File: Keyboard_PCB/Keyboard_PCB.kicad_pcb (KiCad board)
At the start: 6 copper layers, 51 parts, among them J1 Conn_ARM_SWD_TagConnect_TC2030, J2 CH_USB_C, SW1 BOOT, SW10 7, SW11 8, SW12 9, SW13 10, SW14 11, SW2 NRST, SW3 0, SW4 1, SW5 2, SW6 3, SW7 4, SW8 5, SW9 6, U1 EMMC32G-TS0A-01002, U2 STM32U385VGI6, U3 CC2500, U4 USBLC6-2SC6, U5 ISL91127IRAZ, Y1 25MHz, Y2 32.786KHz

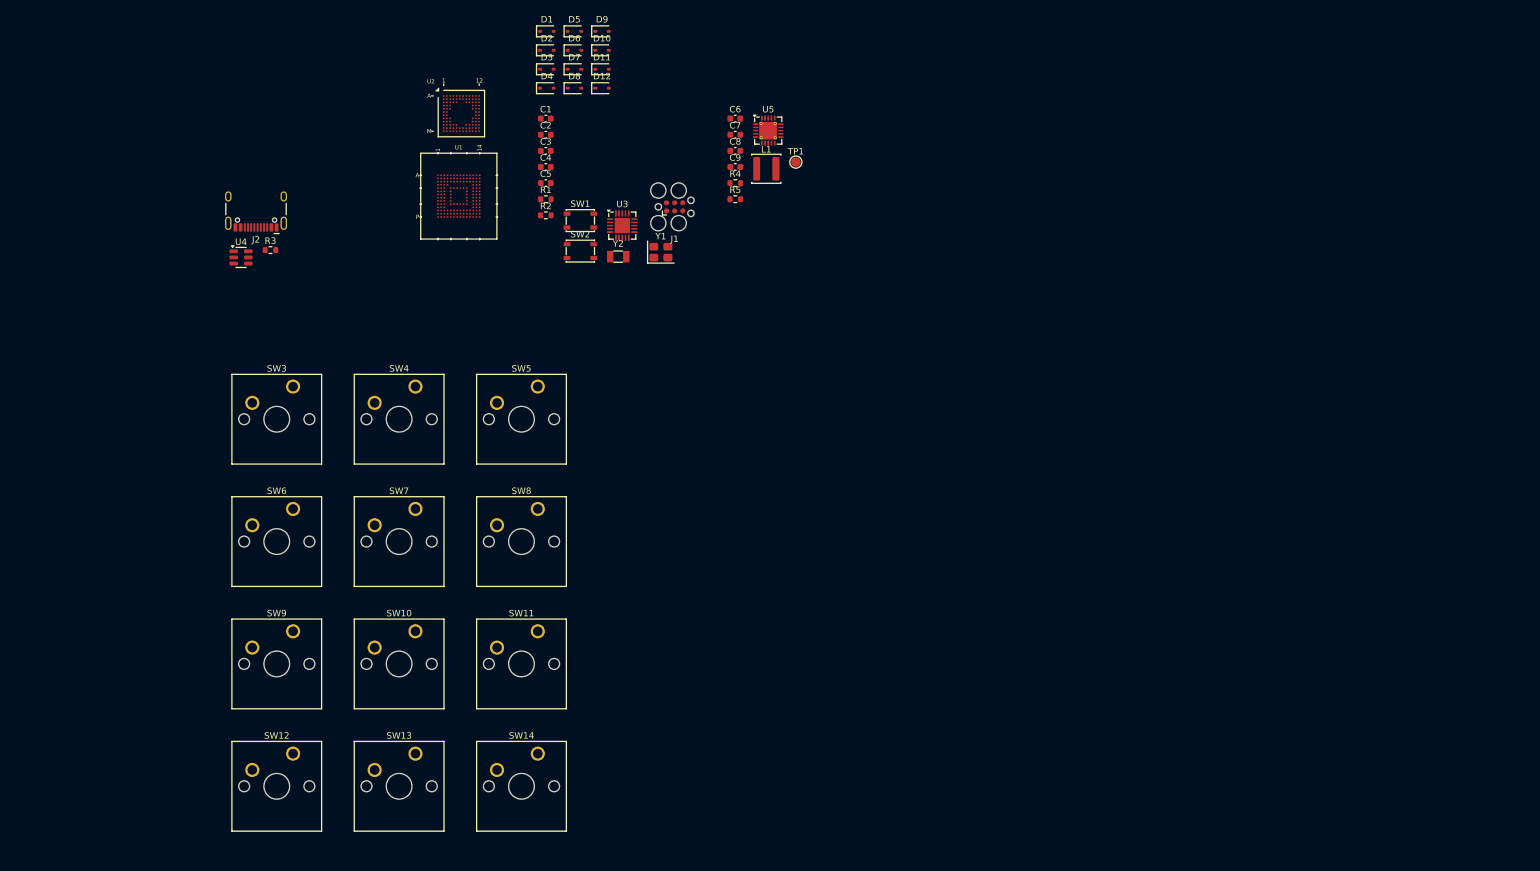
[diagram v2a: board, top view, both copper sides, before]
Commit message: Schematic done
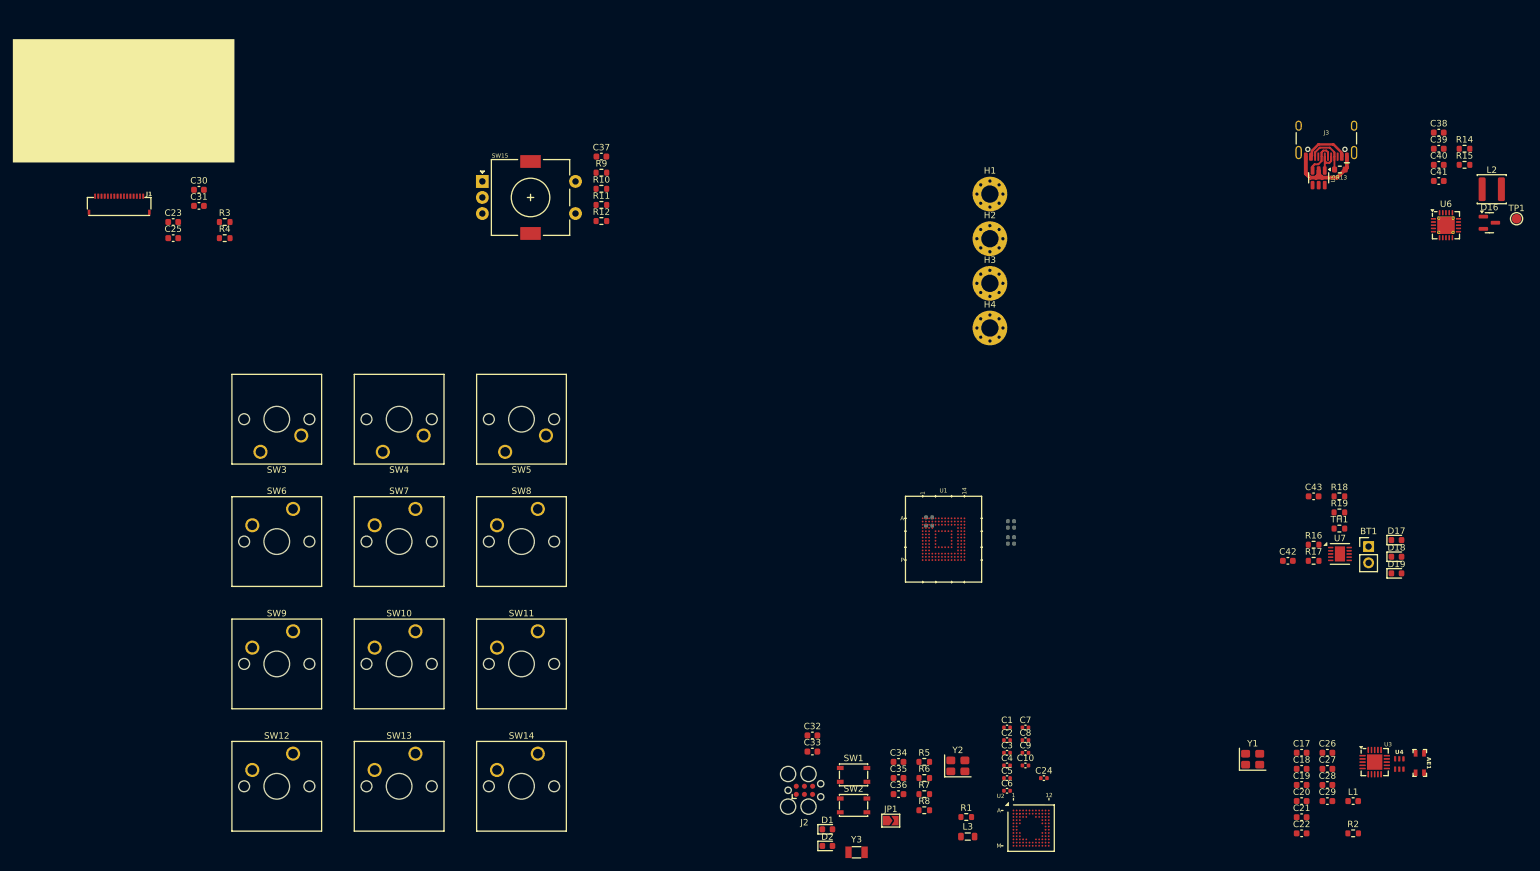
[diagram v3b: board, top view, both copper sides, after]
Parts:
- removed D10, D11, D12, D3, D4, D5, D6, D7, D8, D9: D_Small, Diode_SMD:D_SOD-323
- added AE1: 2450AT18D0100, Marijn:2450AT18D0100, F.Cu at (281.3, 149.2)
- added BT1: APP, Connector_PinHeader_2.54mm:PinHeader_1x02_P2.54mm_Vertical, F.Cu at (273.3, 115.4)
- added C10: 10u, Capacitor_SMD:C_0402_1005Metric, F.Cu at (219.9, 149.5)
- added C11: 4u7, Capacitor_SMD:C_0402_1005Metric, B.Cu at (217.6, 114.0)
- added C12: 4u7, Capacitor_SMD:C_0402_1005Metric, B.Cu at (217.6, 111.5)
- added C13: 4u7, Capacitor_SMD:C_0402_1005Metric, B.Cu at (204.9, 110.9)
- added C14: 100n, Capacitor_SMD:C_0402_1005Metric, B.Cu at (217.6, 115.0)
- added C15: 100n, Capacitor_SMD:C_0402_1005Metric, B.Cu at (217.6, 112.5)
- added C16: 100n, Capacitor_SMD:C_0402_1005Metric, B.Cu at (204.9, 112.2)
- added C17: 220p, Capacitor_SMD:C_0603_1608Metric, F.Cu at (262.9, 147.6)
- added C18: 100n, Capacitor_SMD:C_0603_1608Metric, F.Cu at (262.9, 150.1)
- added C19: 100n, Capacitor_SMD:C_0603_1608Metric, F.Cu at (262.9, 152.6)
- added C20: 220p, Capacitor_SMD:C_0603_1608Metric, F.Cu at (262.9, 155.1)
- added C21: 220p, Capacitor_SMD:C_0603_1608Metric, F.Cu at (262.9, 157.6)
- added C22: 100n, Capacitor_SMD:C_0603_1608Metric, F.Cu at (262.9, 160.1)
- added C23: 1u, Capacitor_SMD:C_0603_1608Metric, F.Cu at (87.2, 64.9)
- added C24: 4u7, Capacitor_SMD:C_0402_1005Metric, F.Cu at (222.7, 151.5)
- added C25: 1u, Capacitor_SMD:C_0603_1608Metric, F.Cu at (87.2, 67.4)
- added C26: 22p, Capacitor_SMD:C_0603_1608Metric, F.Cu at (266.9, 147.6)
- added C27: 100n, Capacitor_SMD:C_0603_1608Metric, F.Cu at (266.9, 150.1)
- added C28: 15p, Capacitor_SMD:C_0603_1608Metric, F.Cu at (266.9, 152.6)
- added C29: 15p, Capacitor_SMD:C_0603_1608Metric, F.Cu at (266.9, 155.1)
- added C30: 10u, Capacitor_SMD:C_0603_1608Metric, F.Cu at (91.2, 59.9)
- added C31: 10u, Capacitor_SMD:C_0603_1608Metric, F.Cu at (91.2, 62.4)
- added C32: 100n, Capacitor_SMD:C_0603_1608Metric, F.Cu at (186.7, 144.9)
- added C33: 12p, Capacitor_SMD:C_0603_1608Metric, F.Cu at (186.7, 147.4)
- added C34: 12p, Capacitor_SMD:C_0603_1608Metric, F.Cu at (200.1, 149.0)
- added C35: 12p, Capacitor_SMD:C_0603_1608Metric, F.Cu at (200.1, 151.5)
- added C36: 12p, Capacitor_SMD:C_0603_1608Metric, F.Cu at (200.1, 154.0)
- added C37: 100n, Capacitor_SMD:C_0603_1608Metric, F.Cu at (153.8, 54.7)
- added C38: 10u, Capacitor_SMD:C_0603_1608Metric, F.Cu at (284.2, 51.0)
- added C39: 56p, Capacitor_SMD:C_0603_1608Metric, F.Cu at (284.2, 53.5)
- added C40: 22u, Capacitor_SMD:C_0603_1608Metric, F.Cu at (284.2, 56.0)
- added C41: 22u, Capacitor_SMD:C_0603_1608Metric, F.Cu at (284.2, 58.5)
- added C42: 1u, Capacitor_SMD:C_0603_1608Metric, F.Cu at (260.7, 117.7)
- added C43: 1u, Capacitor_SMD:C_0603_1608Metric, F.Cu at (264.7, 107.6)
- added D16: BAT54C, Package_TO_SOT_SMD:SOT-23, F.Cu at (292.1, 65.0)
- added D17: STAT1, LED_SMD:LED_0603_1608Metric, F.Cu at (277.6, 114.4)
- added D18: STAT2, LED_SMD:LED_0603_1608Metric, F.Cu at (277.6, 117.0)
- added D19: PG, LED_SMD:LED_0603_1608Metric, F.Cu at (277.6, 119.6)
- added H1: MountingHole_Pad, MountingHole:MountingHole_2.7mm_M2.5_Pad_Via, F.Cu at (214.3, 60.6)
- added H2: MountingHole_Pad, MountingHole:MountingHole_2.7mm_M2.5_Pad_Via, F.Cu at (214.3, 67.5)
- added H3: MountingHole_Pad, MountingHole:MountingHole_2.7mm_M2.5_Pad_Via, F.Cu at (214.3, 74.5)
- added H4: MountingHole_Pad, MountingHole:MountingHole_2.7mm_M2.5_Pad_Via, F.Cu at (214.3, 81.4)
- added J3: CH_USB_C, Connector_USB:USB_C_Receptacle_HCTL_HC-TYPE-C-16P-01A, F.Cu at (266.7, 51.0)
- added JP1: PWR_LED_EN, Jumper:SolderJumper-2_P1.3mm_Open_TrianglePad1.0x1.5mm, F.Cu at (198.9, 158.1)
- added L2: 1u, Inductor_SMD:L_APV_ANR4018, F.Cu at (292.5, 59.8)
- added L3: 10u, Inductor_SMD:L_0805_2012Metric, F.Cu at (210.9, 160.6)
- added R10: 10k, Resistor_SMD:R_0603_1608Metric, F.Cu at (153.8, 59.8)
- added R11: 10k, Resistor_SMD:R_0603_1608Metric, F.Cu at (153.8, 62.3)
- added R12: 10k, Resistor_SMD:R_0603_1608Metric, F.Cu at (153.8, 64.8)
- added R13: 5k1, Resistor_SMD:R_0603_1608Metric, F.Cu at (268.8, 56.8)
- added R14: 1M, Resistor_SMD:R_0603_1608Metric, F.Cu at (288.2, 53.5)
- added R15: 320k, Resistor_SMD:R_0603_1608Metric, F.Cu at (288.2, 56.0)
- added R16: 470, Resistor_SMD:R_0603_1608Metric, F.Cu at (264.7, 115.2)
- added R17: 470, Resistor_SMD:R_0603_1608Metric, F.Cu at (264.7, 117.7)
- added R18: 470, Resistor_SMD:R_0603_1608Metric, F.Cu at (268.7, 107.6)
- added R19: 10k, Resistor_SMD:R_0603_1608Metric, F.Cu at (268.7, 110.1)
- added R6: 5k1, Resistor_SMD:R_0603_1608Metric, F.Cu at (204.1, 151.5)
- added R7: 10k, Resistor_SMD:R_0603_1608Metric, F.Cu at (204.1, 154.0)
- added R8: 1k, Resistor_SMD:R_0603_1608Metric, F.Cu at (204.1, 156.5)
- added R9: 10k, Resistor_SMD:R_0603_1608Metric, F.Cu at (153.8, 57.2)
- added SW15: EC11E15244G1, Marijn:EC11E_rotary_MP_pads, F.Cu at (135.3, 58.6)
- added TH1: 10k, Resistor_SMD:R_0603_1608Metric, F.Cu at (268.7, 112.7)
- added U6: ISL91127IRAZ, Package_DFN_QFN:QFN-20-1EP_4x4mm_P0.5mm_EP2.7x2.7mm_ThermalVias, F.Cu at (285.3, 65.4)
- added U7: MCP73833, Package_DFN_QFN:DFN-10-1EP_3x3mm_P0.5mm_EP1.58x2.35mm, F.Cu at (268.8, 116.6)
- added Y3: 32.786KHz, Crystal:Crystal_SMD_3215-2Pin_3.2x1.5mm, F.Cu at (193.6, 163.1)
- C1: footprint Capacitor_SMD:C_0603_1608Metric -> Capacitor_SMD:C_0402_1005Metric
- C2, C3, C5: value 12p -> 100n; footprint Capacitor_SMD:C_0603_1608Metric -> Capacitor_SMD:C_0402_1005Metric
- C4: value 12p -> 1u; footprint Capacitor_SMD:C_0603_1608Metric -> Capacitor_SMD:C_0402_1005Metric
- C6: value 10u -> 100n; footprint Capacitor_SMD:C_0603_1608Metric -> Capacitor_SMD:C_0402_1005Metric
- C7: value 56p -> 100n; footprint Capacitor_SMD:C_0603_1608Metric -> Capacitor_SMD:C_0402_1005Metric
- C8, C9: value 22u -> 100n; footprint Capacitor_SMD:C_0603_1608Metric -> Capacitor_SMD:C_0402_1005Metric
- D1: value D_Small -> PWR; footprint Diode_SMD:D_SOD-323 -> LED_SMD:LED_0603_1608Metric
- D2: value D_Small -> CH_STATUS; footprint Diode_SMD:D_SOD-323 -> LED_SMD:LED_0603_1608Metric
- J1: value Conn_ARM_SWD_TagConnect_TC2030 -> ~; footprint Connector:Tag-Connect_TC2030-IDC-FP_2x03_P1.27mm_Vertical -> Marijn:FFC2B28-16-G
- J2: value CH_USB_C -> Conn_ARM_SWD_TagConnect_TC2030; footprint Connector_USB:USB_C_Receptacle_HCTL_HC-TYPE-C-16P-01A -> Connector:Tag-Connect_TC2030-IDC-FP_2x03_P1.27mm_Vertical
- L1: value 1u -> 10n; footprint Inductor_SMD:L_APV_ANR4018 -> Inductor_SMD:L_0603_1608Metric
- R2: value 10k -> 56k
- R4: value 1M -> 680K
- R5: value 320k -> 10k
- U4: value USBLC6-2SC6 -> 2450BM15B0003001E; footprint Package_TO_SOT_SMD:SOT-23-6 -> Marijn:2450BM15B0003001E
- U5: value ISL91127IRAZ -> USBLC6-2SC6; footprint Package_DFN_QFN:QFN-20-1EP_4x4mm_P0.5mm_EP2.7x2.7mm_ThermalVias -> Package_TO_SOT_SMD:SOT-23-6
- Y1: value 25MHz -> 26MHz
- Y2: value 32.786KHz -> 25MHz; footprint Crystal:Crystal_SMD_3215-2Pin_3.2x1.5mm -> Crystal:Crystal_SMD_3225-4Pin_3.2x2.5mm
- moved U4 196.8 mm to (278.1, 149.3)
- moved R2 158.3 mm to (270.9, 160.1)
- moved U3 143.9 mm to (274.2, 149.0)
- moved U2 142.3 mm to (220.7, 159.3)
- moved L1 134.3 mm to (270.9, 155.1)
- moved D1 131.7 mm to (189.0, 159.5)
- moved D2 131.3 mm to (189.0, 162.1)
- moved J2 125.1 mm to (185.5, 153.4), turned to 0 degrees
- moved Y1 121.3 mm to (255.2, 148.6)
- moved C1 118.9 mm to (217.0, 143.6)
- moved C2 118.5 mm to (217.0, 145.6)
- moved C3 118.1 mm to (217.0, 147.6)
- moved C4 117.6 mm to (217.0, 149.5)
- moved C5 117.2 mm to (217.0, 151.5)
- moved R1 116.3 mm to (210.6, 157.6)
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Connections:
- C1 pad 2: /NRST -> +3V3
- C2 pad 2: /HSE_I -> +3V3
- C3 pad 2: /HSE_O -> +3.3VA
- C4 pad 2: /LSE_I -> +3.3VA
- C5 pad 2: /LSE_O -> +3V3
- C6 pad 1: /PWR/VBUS -> GND
- C6 pad 2: GND -> +3V3
- C7 pad 1: +3V3 -> GND
- C7 pad 2: Net-(U5-FB) -> +3V3
- C8 pad 1: +3V3 -> GND
- C8 pad 2: GND -> +3V3
- C9 pad 1: +3V3 -> GND
- C9 pad 2: GND -> +3V3
- D1 pad 1: /ROW_0 -> GND
- D2 pad 1: /ROW_0 -> /STATUS
- J1 pad 1: +3V3 -> Net-(C23-Pad1)
- J1 pad 2: /SWDIO -> Net-(C23-Pad2)
- J1 pad 3: /NRST -> Net-(C25-Pad1)
- J1 pad 4: /SWCLK -> Net-(C25-Pad2)
- J1 pad 5: GND -> +3V3
- J1 pad 6: /SWO -> GND
- L1 pad 1: Net-(L1-Pad1) -> Net-(U3-RF_P)
- L1 pad 2: Net-(L1-Pad2) -> Net-(U3-RF_N)
- R1 pad 1: /NRST -> /BAT
- R1 pad 2: +3V3 -> Net-(U2-PC0)
- R2 pad 2: /BOOT -> Net-(U3-RBIAS)
- R3 pad 1: Net-(J2-CC1) -> GND
- R3 pad 2: GND -> /OLED_RST
- R4 pad 1: +3V3 -> Net-(J1-Pad13)
- R4 pad 2: Net-(U5-FB) -> GND
- R5 pad 1: GND -> /NRST
- R5 pad 2: Net-(U5-FB) -> +3V3
- SW3 pad 2: Net-(D1-A) -> Net-(D3-A)
- SW4 pad 2: Net-(D2-A) -> Net-(D4-A)
- U1 pad C2: unconnected-(U1-VDD_i-PadC2) -> Net-(U1-VDD_i)
- U2 pad A9: unconnected-(U2-PA15-PadA9) -> /STATUS
- U2 pad C11: unconnected-(U2-VDDUSB-PadC11) -> +3V3
- U2 pad C4: unconnected-(U2-VDD-PadC4) -> +3V3
- U2 pad D3: unconnected-(U2-VSS-PadD3) -> GND
- U2 pad E2: unconnected-(U2-VBAT-PadE2) -> +3V3
- U2 pad E3: unconnected-(U2-VSS-PadE3) -> GND
- U2 pad F11: unconnected-(U2-VSS-PadF11) -> GND
- U2 pad F12: unconnected-(U2-VSS-PadF12) -> GND
- U2 pad F2: unconnected-(U2-VSS-PadF2) -> GND
- U2 pad G11: unconnected-(U2-VDD-PadG11) -> +3V3
- U2 pad G12: unconnected-(U2-VDD-PadG12) -> +3V3
- U2 pad G2: unconnected-(U2-VDD-PadG2) -> +3V3
- U2 pad H1: unconnected-(U2-PC0-PadH1) -> Net-(U2-PC0)
- U2 pad H12: unconnected-(U2-PD13-PadH12) -> /ROT_A
- U2 pad H3: unconnected-(U2-VDD-PadH3) -> +3V3
- U2 pad J1: unconnected-(U2-VSSA-PadJ1) -> GND
- U2 pad J12: unconnected-(U2-PD10-PadJ12) -> /ROT_B
- U2 pad K1: unconnected-(U2-VREF--PadK1) -> GND
- U2 pad K11: /OLED_SPI_NSS -> unconnected-(U2-PB14-PadK11)
- U2 pad L1: unconnected-(U2-VREF+-PadL1) -> +3.3VA
- U2 pad L11: unconnected-(U2-VCAP-PadL11) -> Net-(U2-VCAP)
- U2 pad L12: unconnected-(U2-PB12-PadL12) -> /OLED_SPI_NSS
- U2 pad L2: unconnected-(U2-PA0-PadL2) -> /ROT_SW
- U2 pad M1: unconnected-(U2-VDDA-PadM1) -> +3.3VA
- U3 pad 1: /SPI_SCK -> /RF_SPI_SCK
- U3 pad 10: unconnected-(U3-XOSC_Q2-Pad10) -> Net-(U3-XOSC_Q2)
- U3 pad 11: Net-(U3-AVDD-Pad11) -> +3V3
- U3 pad 12: unconnected-(U3-RF_P-Pad12) -> Net-(U3-RF_P)
- U3 pad 13: unconnected-(U3-RF_N-Pad13) -> Net-(U3-RF_N)
- U3 pad 14: Net-(U3-AVDD-Pad11) -> +3V3
- U3 pad 15: Net-(U3-AVDD-Pad11) -> +3V3
- U3 pad 17: unconnected-(U3-RBIAS-Pad17) -> Net-(U3-RBIAS)
- U3 pad 18: unconnected-(U3-VDD_GUARD-Pad18) -> +3V3
- U3 pad 2: /SPI_MISO -> /RF_SPI_MISO
- U3 pad 20: /SPI_MOSI -> /RF_SPI_MOSI
- U3 pad 4: unconnected-(U3-DVDD-Pad4) -> +3V3
- U3 pad 5: unconnected-(U3-DCOUPL-Pad5) -> Net-(U3-DCOUPL)
- U3 pad 7: /SPI_NSS -> /RF_SPI_NSS
- U3 pad 8: unconnected-(U3-XOSC_Q1-Pad8) -> Net-(U3-XOSC_Q1)
- U3 pad 9: Net-(U3-AVDD-Pad11) -> +3V3
- U4 pad 1: Net-(J2-D--PadA7) -> Net-(AE1-FEED)
- U4 pad 2: GND -> Net-(U4-CAP)
- U4 pad 3: Net-(J2-D+-PadA6) -> Net-(U3-RF_N)
- U4 pad 4: /USB_DP -> Net-(U3-RF_P)
- U4 pad 5: /PWR/VBUS -> GND
- U4 pad 6: /USB_DN -> GND
- U5 pad 1: Net-(L1-Pad2) -> Net-(J3-D--PadA7)
- U5 pad 2: Net-(L1-Pad2) -> GND
- U5 pad 3: GND -> Net-(J3-D+-PadA6)
- U5 pad 4: Net-(L1-Pad1) -> /USB_DP
- U5 pad 5: Net-(L1-Pad1) -> /PWR/VBUS
- U5 pad 6: /PWR/VBUS -> /USB_DN
- Y1 pad 1: /HSE_I -> Net-(U3-XOSC_Q1)
- Y1 pad 3: /HSE_O -> Net-(U3-XOSC_Q2)
- Y2 pad 1: /LSE_I -> /HSE_I
- Y2 pad 2: /LSE_O -> GND
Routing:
- net GND: track 0.00 -> 14.3 mm
- net /PWR/VBUS: track 0.00 -> 7.17 mm
- net Net-(J3-CC1): track 0.00 -> 6.98 mm
- net Net-(J3-D+-PadA6): track 0.00 -> 5.67 mm
- net Net-(J3-D--PadA7): track 0.00 -> 4.74 mm

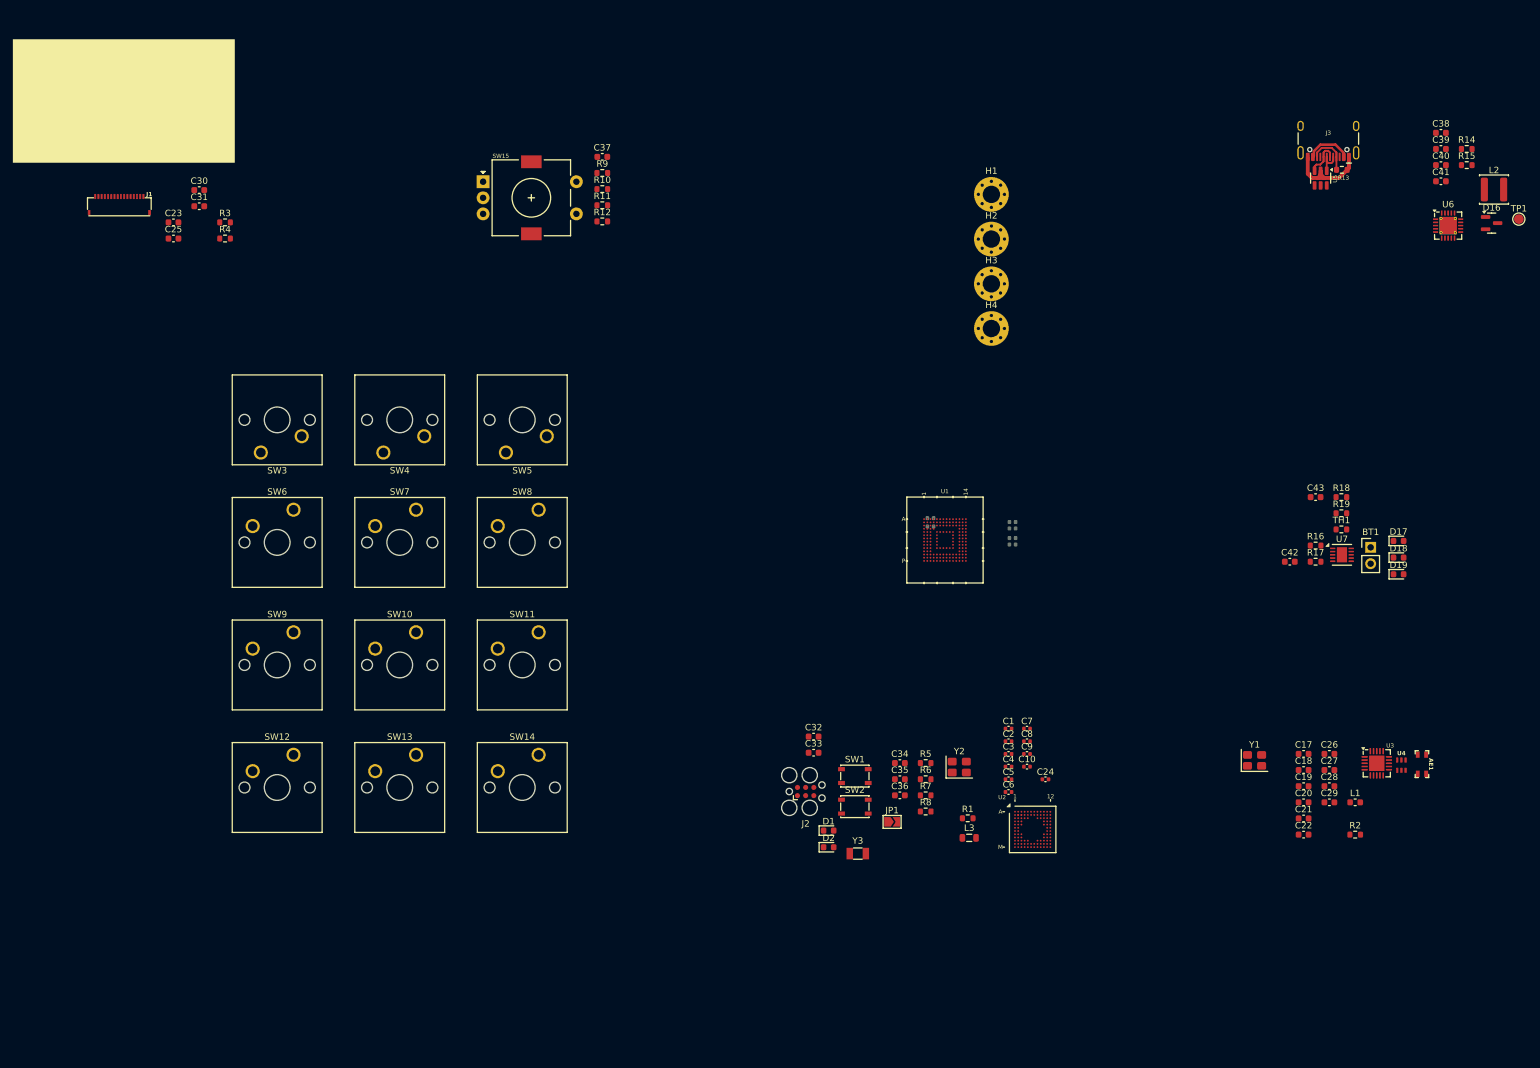
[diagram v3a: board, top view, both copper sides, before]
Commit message: eMMC routing and STM passives
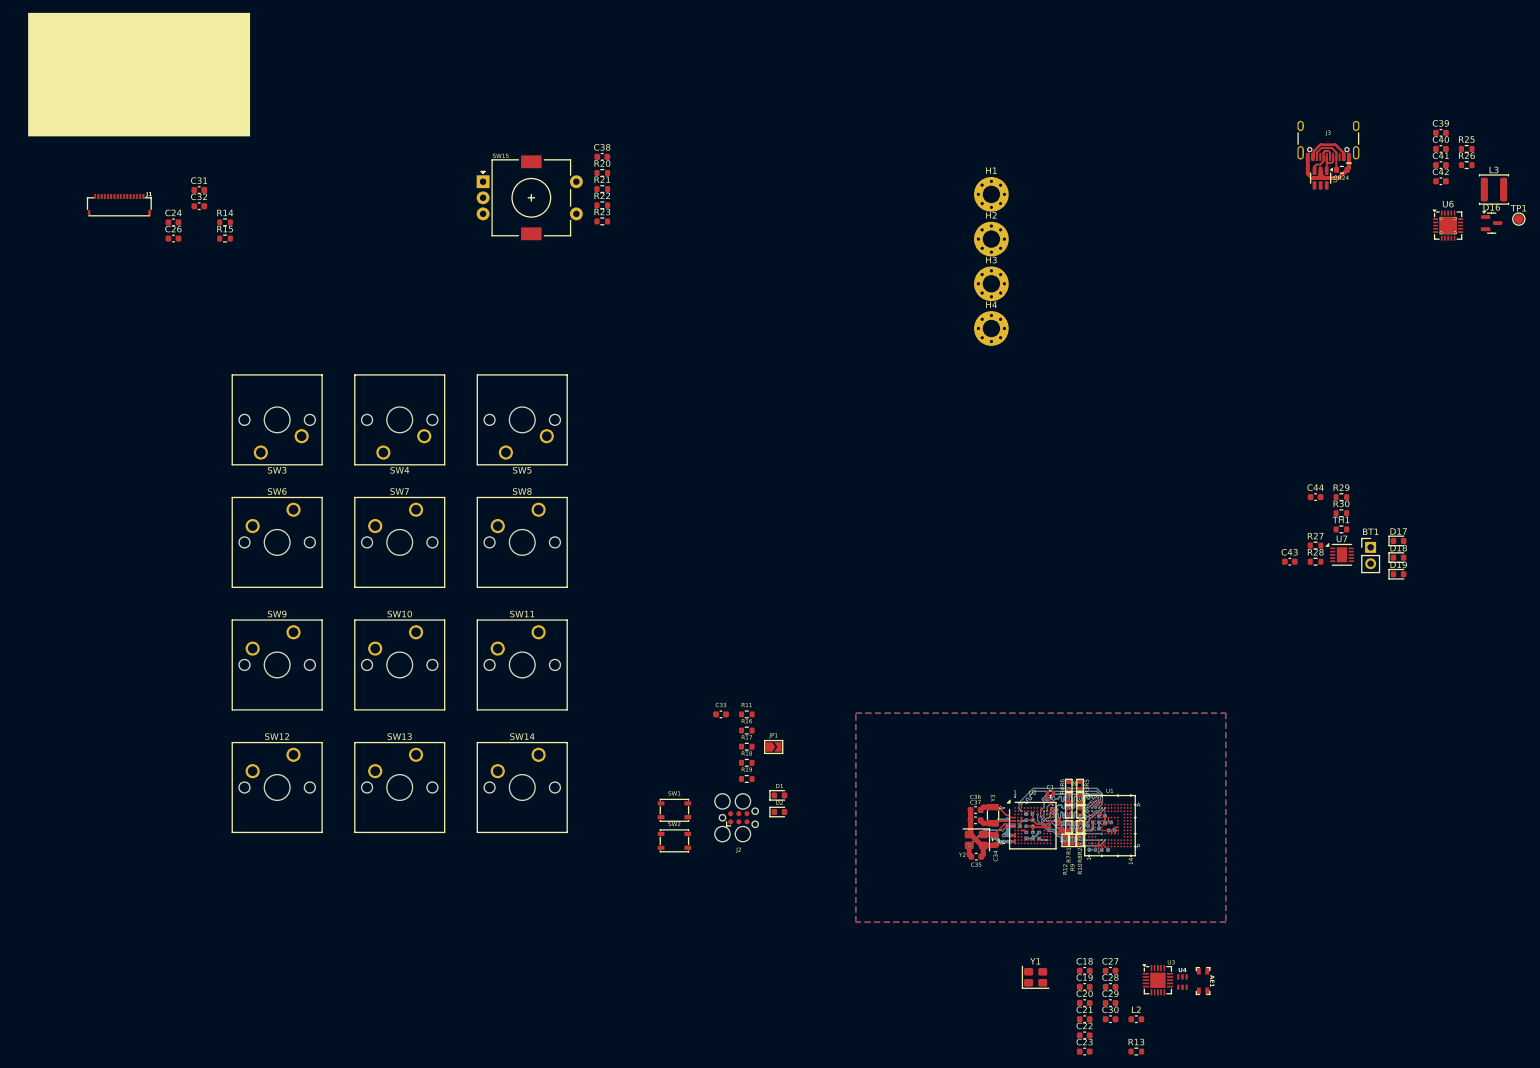
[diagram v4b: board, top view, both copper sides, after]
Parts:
- removed the C24 at (222.7, 151.5)
- removed the C32 at (186.7, 144.9)
- removed the L3 at (210.9, 160.6)
- added C17: 100n, Capacitor_SMD:C_0402_1005Metric, B.Cu at (230.6, 158.2)
- added C25: 4u7, Capacitor_SMD:C_0402_1005Metric, B.Cu at (221.8, 160.2)
- added C37: 12p, Capacitor_SMD:C_0603_1608Metric, F.Cu at (211.9, 157.9)
- added L1: 10u, Inductor_SMD:L_0805_2012Metric, B.Cu at (214.9, 159.5)
- added R10: 22, PCM_Resistor_SMD_AKL:R_0402_1005Metric, F.Cu at (228.1, 161.0)
- added R11: 10k, Resistor_SMD:R_0603_1608Metric, F.Cu at (176.3, 141.4)
- added R12: 50k, PCM_Resistor_SMD_AKL:R_0402_1005Metric, F.Cu at (225.8, 161.0)
- added R16: 10k, Resistor_SMD:R_0603_1608Metric, F.Cu at (176.3, 143.9)
- added R17: 5k1, Resistor_SMD:R_0603_1608Metric, F.Cu at (176.3, 146.4)
- added R18: 10k, Resistor_SMD:R_0603_1608Metric, F.Cu at (176.3, 148.9)
- added R19: 1k, Resistor_SMD:R_0603_1608Metric, F.Cu at (176.3, 151.5)
- added R2: 50k, PCM_Resistor_SMD_AKL:R_0402_1005Metric, F.Cu at (228.1, 156.6)
- added R3: 50k, PCM_Resistor_SMD_AKL:R_0402_1005Metric, F.Cu at (228.1, 154.5)
- added R4: 50k, PCM_Resistor_SMD_AKL:R_0402_1005Metric, F.Cu at (226.4, 154.5)
- added R9: 10k, PCM_Resistor_SMD_AKL:R_0402_1005Metric, F.Cu at (227.0, 161.0)
- C10, C2, C3, C4, C5, C6, C7, C8, C9: moved to B.Cu
- C11: value 4u7 -> 100n
- C12: value 4u7 -> 2u2
- C13: value 4u7 -> 1u
- C14, C16: value 100n -> 2u2
- C33: value 12p -> 100n
- R1, R5, R7: value 10k -> 50k; footprint Resistor_SMD:R_0603_1608Metric -> PCM_Resistor_SMD_AKL:R_0402_1005Metric
- R6: value 5k1 -> 50k; footprint Resistor_SMD:R_0603_1608Metric -> PCM_Resistor_SMD_AKL:R_0402_1005Metric
- R8: value 1k -> 50k; footprint Resistor_SMD:R_0603_1608Metric -> PCM_Resistor_SMD_AKL:R_0402_1005Metric
- U1: value EMMC32G-TS0A-01002 -> S40FC002C1B2I00000; footprint Marijn:FBGA153_13X11.5X0.8 -> Marijn:FBGA153_9x7.5x0.8
- moved C13 57.4 mm to (230.0, 162.5), turned to 0 degrees
- moved C16 52.3 mm to (231.5, 157.2), turned to 0 degrees
- moved U1 51.3 mm to (232.8, 158.7)
- moved C11 50.5 mm to (232.0, 162.5)
- moved C12 50.4 mm to (233.0, 159.5), turned to 0 degrees
- moved C15 48.1 mm to (232.5, 158.2)
- moved U4 47.9 mm to (244.0, 183.0)
- moved C18 47.9 mm to (228.8, 181.3)
- moved C21 47.9 mm to (228.8, 188.8)
- moved C27 47.9 mm to (232.8, 181.3)
- moved C30 47.9 mm to (232.8, 188.8)
- moved L2 47.9 mm to (236.9, 188.8)
- moved AE1 47.9 mm to (247.2, 182.9)
- moved C19 47.9 mm to (228.8, 183.8)
- moved C20 47.9 mm to (228.8, 186.3)
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- renumbered C17 to C18, C18 to C19, C19 to C20, C20 to C21, C21 to C22, C22 to C23, C23 to C24, C25 to C26, C26 to C27, C27 to C28, C28 to C29, C29 to C30, C30 to C31, C31 to C32, C37 to C38, C38 to C39, C39 to C40, C40 to C41, C41 to C42, C42 to C43, C43 to C44, L1 to L2, L2 to L3, R2 to R13, R3 to R14, R4 to R15, R9 to R20, R10 to R21, R11 to R22, R12 to R23, R13 to R24, R14 to R25, R15 to R26, R16 to R27, R17 to R28, R18 to R29, R19 to R30
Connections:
- C11 pad 2: VCC -> VCC_q
- C12 pad 2: VCC_q -> VCC
- C13 pad 2: Net-(U1-VDD_i) -> VCC_q
- C14 pad 2: VCC -> /VCCI
- C15 pad 2: VCC_q -> VCC
- C16 pad 2: Net-(U1-VDD_i) -> VCC_q
- C33 pad 2: /HSE_I -> /NRST
- C34 pad 2: /HSE_O -> /HSE_I
- C35 pad 2: /LSE_I -> /HSE_O
- C36 pad 2: /LSE_O -> /LSE_I
- R1 pad 1: /BAT -> /eMMC_D0
- R1 pad 2: Net-(U2-PC0) -> +3V3
- R5 pad 1: /NRST -> /eMMC_D4
- R6 pad 1: Net-(JP1-B) -> /eMMC_D5
- R6 pad 2: Net-(D1-A) -> +3V3
- R7 pad 1: GND -> /eMMC_D6
- R7 pad 2: /BOOT -> +3V3
- R8 pad 1: +3V3 -> /eMMC_D7
- R8 pad 2: Net-(D2-A) -> +3V3
- U1 pad C2: Net-(U1-VDD_i) -> /VCCI
- U1 pad M6: /eMMC_CLK -> Net-(U1-CLK)
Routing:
- net GND: track 14.3 -> 55.1 mm, vias 0 -> 17
- net /eMMC_D7: track 0.00 -> 19.1 mm, vias 0 -> 3
- net /eMMC_D6: track 0.00 -> 18.6 mm, vias 0 -> 3
- net /eMMC_D3: track 0.00 -> 18.6 mm, vias 0 -> 3
- net /eMMC_D4: track 0.00 -> 18.3 mm, vias 0 -> 3
- net /eMMC_CMD: track 0.00 -> 18.2 mm, vias 0 -> 3
- net /eMMC_D5: track 0.00 -> 18.2 mm, vias 0 -> 3
- net /eMMC_D0: track 0.00 -> 18.2 mm, vias 0 -> 3
- net /eMMC_D2: track 0.00 -> 18.1 mm, vias 0 -> 3
- net /eMMC_D1: track 0.00 -> 17.8 mm, vias 0 -> 3
- net /eMMC_NRST: track 0.00 -> 16.4 mm, vias 0 -> 2
- net +3V3: track 0.00 -> 15.9 mm, vias 0 -> 14
- net /HSE_O: track 0.00 -> 10.2 mm, vias 0 -> 2
- net /eMMC_CLK: track 0.00 -> 9.92 mm, vias 0 -> 2
- net /LSE_I: track 0.00 -> 6.24 mm
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- added copper zone on F.Cu, net +3V3
- added copper zone on In3.Cu, net +3V3
- added copper zone on B.Cu, net GND
- added copper zone on F.Cu, net GND
- added copper zone on In1.Cu, net GND
- added copper zone on In4.Cu, net GND
